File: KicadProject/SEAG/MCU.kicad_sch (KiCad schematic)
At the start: 13 parts, among them J2 Conn_01x06_Pin, SW1 SW_SPDT, U1 STM32F722RCTx, Y1 Crystal_GND24

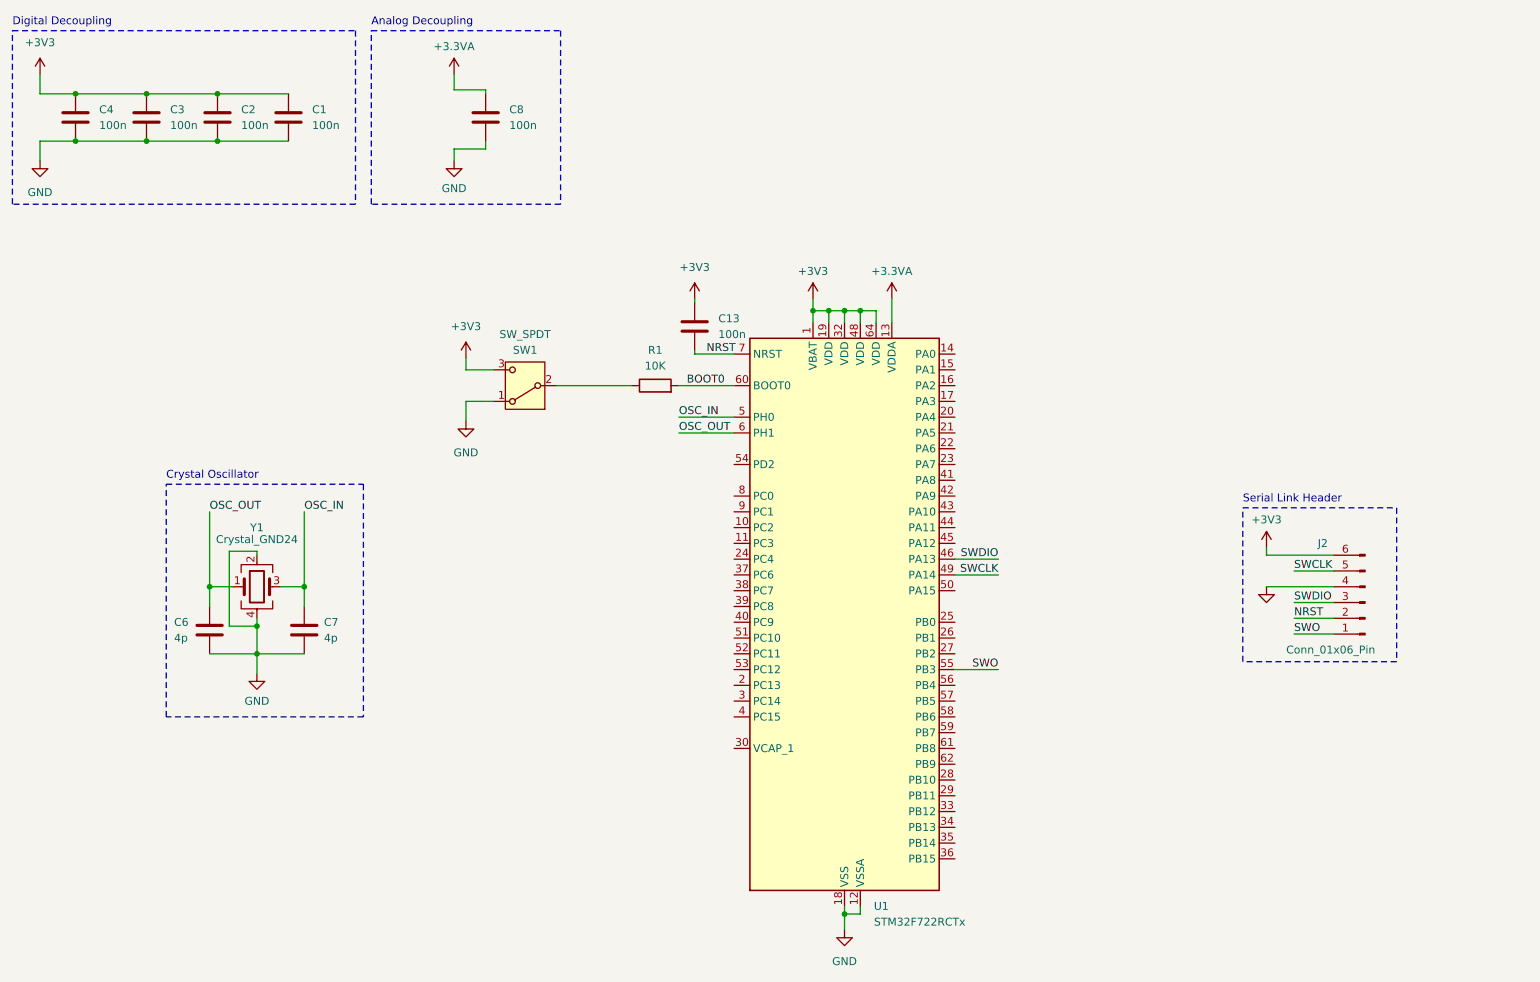
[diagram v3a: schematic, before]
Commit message: Finished PCB, stil uncertain about couple things
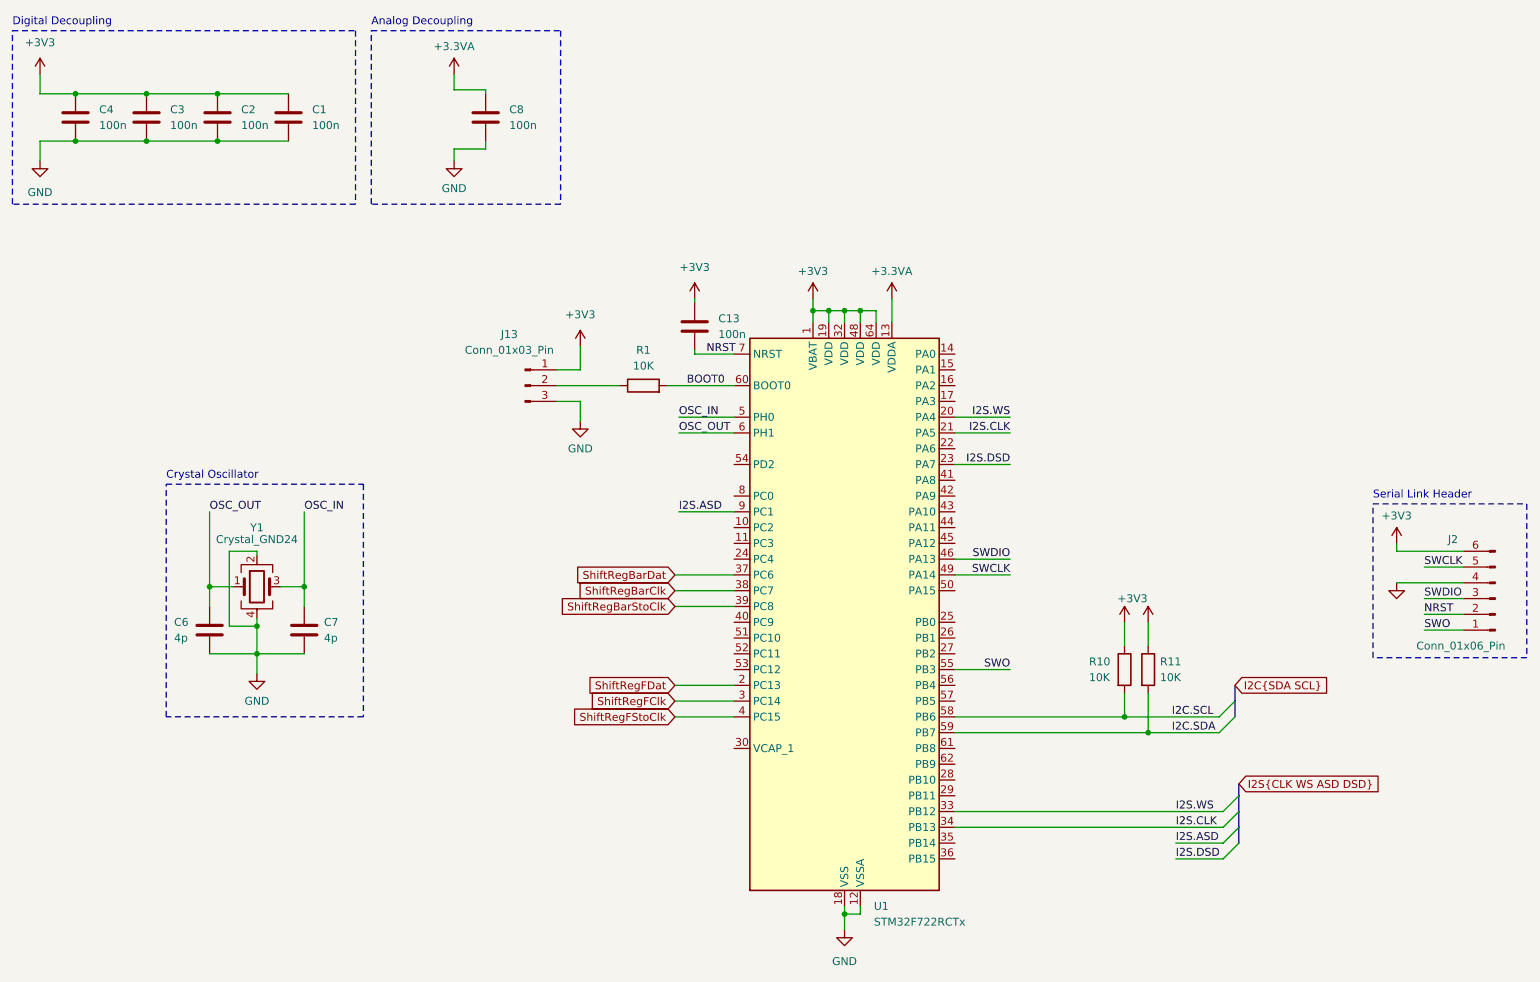
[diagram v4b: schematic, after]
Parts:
- removed SW1: SW_SPDT, symbol Switch:SW_SPDT
- added J13: Conn_01x03_Pin, Connector_PinHeader_2.54mm:PinHeader_1x03_P2.54mm_Vertical, symbol Connector:Conn_01x03_Pin
- added R10, R11: 10K, Resistor_SMD:R_0805_2012Metric, symbol Device:R
- Y1: footprint (none) -> SamacSys_Parts:FW2500025Z
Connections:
- net +3V3: now also J13.1 (Pin_1), R10.1, R11.1
- net GND: now also J13.3 (Pin_3)
- net at R1.1: now also J13.2 (Pin_2)
- net ShiftRegFDat: now reaches U1.2 (PC13)
- net I2S.WS: now reaches U1.20 (PA4)
- net I2S.WS: now also U1.33 (PB12)
- net I2S.CLK: now reaches U1.21 (PA5)
- net I2S.CLK: now also U1.34 (PB13)
- net I2S.DSD: now reaches U1.23 (PA7)
- net ShiftRegFClk: now reaches U1.3 (PC14)
- net ShiftRegBarDat: now reaches U1.37 (PC6)
- net ShiftRegBarClk: now reaches U1.38 (PC7)
- net ShiftRegBarStoClk: now reaches U1.39 (PC8)
- net ShiftRegFStoClk: now reaches U1.4 (PC15)
- net I2C.SCL: now reaches U1.58 (PB6)
- net I2C.SCL: now also R10.2
- net I2C.SDA: now reaches U1.59 (PB7)
- net I2C.SDA: now also R11.2
- net I2S.ASD: now reaches U1.9 (PC1)
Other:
- moved on the sheet: J2, R1

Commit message: PCB rev 2
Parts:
- removed J13: Conn_01x03_Pin, Connector_PinHeader_2.54mm:PinHeader_1x03_P2.54mm_Vertical, symbol Connector:Conn_01x03_Pin
- added C305: 100n, Capacitor_SMD:C_0805_2012Metric, symbol Device:C
- added C309: 4.7u, Capacitor_SMD:C_0805_2012Metric, symbol Device:C
- added H1, H2, H3, H4: MountingHole, MountingHole:MountingHole_3mm, symbol Mechanical:MountingHole
- renumbered C4 to C301, C3 to C302, C2 to C303, C1 to C304, C8 to C306, C6 to C307, C7 to C308, R1 to R301, R10 to R302, R11 to R303
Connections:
- net +3V3: now also C305.1
- net GND: now also R301.1, C305.2, C309.2
- net ShiftRegBarClk: now also U1.10 (PC2); no longer U1.38 (PC7)
- net ShiftRegBarDat: now also U1.8 (PC0); no longer U1.37 (PC6)
- net ShiftRegBarStoClk: now also U1.11 (PC3); no longer U1.39 (PC8)
- net MCLK: now reaches U1.24 (PC4)
- net at U1.30 (VCAP_1): now also C309.1
- net ToggleInput2: now reaches U1.42 (PA9)
- net ToggleInput1: now reaches U1.43 (PA10)
- net ToggleInput4: now reaches U1.44 (PA11)
- net ToggleInput3: now reaches U1.45 (PA12)
- net ToggleInput8: now reaches U1.50 (PA15)
- net ToggleInput7: now reaches U1.51 (PC10)
- net ToggleInput6: now reaches U1.52 (PC11)
- net ToggleInput5: now reaches U1.53 (PC12)
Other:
- moved on the sheet: C306, J2

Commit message: Slight PCB changes
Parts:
- removed H1, H2, H3, H4: MountingHole, MountingHole:MountingHole_3mm, symbol Mechanical:MountingHole
- added C311: 1u, Capacitor_SMD:C_0805_2012Metric, symbol Device:C
- renumbered C13 to C310
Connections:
- net +3V3: now also C311.1
- net GND: now also C311.2
- net RotEncoderIn1: now reaches U1.37 (PC6)
- net RotEncoderIn2: now reaches U1.38 (PC7)
- net RotEncoderButton: now reaches U1.39 (PC8)
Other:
- moved on the sheet: C306

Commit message: Added header
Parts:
- added J9: Conn_01x06_Pin, Connector_PinHeader_2.54mm:PinHeader_1x06_P2.54mm_Vertical, symbol Connector:Conn_01x06_Pin
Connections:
- net I2C.SCL: now also J9.1 (Pin_1)
- net I2C.SDA: now also J9.2 (Pin_2)
- net I2S.ASD: now also J9.4 (Pin_4)
- net I2S.CLK: now also J9.6 (Pin_6)
- net I2S.DSD: now also J9.3 (Pin_3)
- net I2S.WS: now also J9.5 (Pin_5)
- no-connect marks 0 -> 19
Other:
- note added: "Bus Debug"
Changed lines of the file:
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@@
   (junction (at 42.545 30.48) (diameter 0) (color 0 0 0 0)
   )
+  (no_connect (at 172.72 140.97))
+  (no_connect (at 172.72 125.73))
+  (no_connect (at 172.72 87.63))
+  (no_connect (at 172.72 138.43))
+  (no_connect (at 172.72 135.89))
+  (no_connect (at 172.72 77.47))
+  (no_connect (at 172.72 115.57))
+  (no_connect (at 172.72 118.11))
+  (no_connect (at 137.16 90.17))
+  (no_connect (at 172.72 92.71))
+  (no_connect (at 137.16 115.57))
+  (no_connect (at 172.72 72.39))
+  (no_connect (at 172.72 80.01))
+  (no_connect (at 172.72 120.65))
+  (no_connect (at 172.72 153.67))
+  (no_connect (at 172.72 143.51))
+  (no_connect (at 172.72 151.13))
+  (no_connect (at 172.72 128.27))
+  (no_connect (at 172.72 74.93))
   (bus_entry (at 218.44 146.05) (size -2.54 2.54)
     (stroke (width 0) (type default))
   )
+  (bus_entry (at 243.84 61.595) (size 2.54 2.54)
+    (stroke (width 0) (type default))
+  )
+  (bus_entry (at 243.84 64.135) (size 2.54 2.54)
+    (stroke (width 0) (type default))
+  )
   (bus_entry (at 218.44 148.59) (size -2.54 2.54)
     (stroke (width 0) (type default))
@@
     (stroke (width 0) (type default))
   )
+  (bus_entry (at 243.84 59.055) (size 2.54 2.54)
+    (stroke (width 0) (type default))
+  )
+  (bus_entry (at 243.84 56.515) (size 2.54 2.54)
+    (stroke (width 0) (type default))
+  )
+  (bus_entry (at 243.84 51.435) (size 2.54 2.54)
+    (stroke (width 0) (type default))
+  )
+  (bus_entry (at 243.84 53.975) (size 2.54 2.54)
+    (stroke (width 0) (type default))
+  )
   (wire (pts (xy 127.635 107.95) (xy 137.16 107.95))
     (stroke (width 0) (type default))
   )
+  (wire (pts (xy 246.38 61.595) (xy 254.635 61.595))
+    (stroke (width 0) (type default))
+  )
   (wire (pts (xy 208.28 153.67) (xy 215.9 153.67))
     (stroke (width 0) (type default))
@@
     (stroke (width 0) (type default))
   )
+  (wire (pts (xy 246.38 66.675) (xy 254.635 66.675))
+    (stroke (width 0) (type default))
+  )
   (wire (pts (xy 203.835 127) (xy 203.835 133.35))
     (stroke (width 0) (type default))
@@
     (stroke (width 0) (type default))
   )
+  (wire (pts (xy 246.38 53.975) (xy 254.635 53.975))
+    (stroke (width 0) (type default))
+  )
   (wire (pts (xy 243.84 97.155) (xy 254.635 97.155))
     (stroke (width 0) (type default))
@@
     (stroke (width 0) (type default))
   )
+  (bus (pts (xy 243.84 53.975) (xy 243.84 56.515))
+    (stroke (width 0) (type default))
+  )
   (wire (pts (xy 25.4 27.305) (xy 25.4 30.48))
     (stroke (width 0) (type default))
@@
     (stroke (width 0) (type default))
   )
+  (bus (pts (xy 243.84 48.895) (xy 243.84 51.435))
+    (stroke (width 0) (type default))
+  )
   (wire (pts (xy 126.365 38.1) (xy 126.365 39.37))
     (stroke (width 0) (type default))
@@
     (stroke (width 0) (type default))
   )
+  (bus (pts (xy 243.84 56.515) (xy 243.84 59.055))
+    (stroke (width 0) (type default))
+  )
   (wire (pts (xy 160.02 65.405) (xy 160.02 67.31))
     (stroke (width 0) (type default))
@@
     (stroke (width 0) (type default))
   )
+  (wire (pts (xy 246.38 64.135) (xy 254.635 64.135))
+    (stroke (width 0) (type default))
+  )
   (wire (pts (xy 200.025 117.475) (xy 200.025 119.38))
     (stroke (width 0) (type default))
@@
     (stroke (width 0) (type default))
   )
+  (bus (pts (xy 243.84 61.595) (xy 243.84 64.135))
+    (stroke (width 0) (type default))
+  )
   (wire (pts (xy 31.115 30.48) (xy 42.545 30.48))
     (stroke (width 0) (type default))
@@
     (stroke (width 0) (type default))
   )
+  (bus (pts (xy 243.84 51.435) (xy 243.84 53.975))
+    (stroke (width 0) (type default))
+  )
   (wire (pts (xy 157.48 162.56) (xy 157.48 161.29))
     (stroke (width 0) (type default))
@@
     (stroke (width 0) (type default))
   )
+  (wire (pts (xy 246.38 56.515) (xy 254.635 56.515))
+    (stroke (width 0) (type default))
+  )
   (wire (pts (xy 172.72 146.05) (xy 215.9 146.05))
     (stroke (width 0) (type default))
   )
   (wire (pts (xy 60.325 114.935) (xy 60.325 116.205))
+    (stroke (width 0) (type default))
+  )
+  (wire (pts (xy 246.38 59.055) (xy 254.635 59.055))
+    (stroke (width 0) (type default))
+  )
+  (bus (pts (xy 243.84 60.96) (xy 243.84 61.595))
     (stroke (width 0) (type default))
   )
@@
     (fill (type none))
   )
+  (rectangle (start 218.44 46.355) (end 262.89 71.12)
+    (stroke (width 0) (type dash))
+    (fill (type none))
+  )
   (rectangle (start 240.03 89.535) (end 264.795 114.3)
     (stroke (width 0) (type dash))
@@
     (effects (font (size 1.27 1.27)) (justify left bottom))
   )
+  (text "Bus Debug" (at 218.44 45.72 0)
+    (effects (font (size 1.27 1.27)) (justify left bottom))
+  )
   (label "OSC_IN" (at 67.945 97.79 0) (fields_autoplaced)
     (effects (font (size 1.27 1.27)) (justify left bottom))
@@
     (effects (font (size 1.27 1.27)) (justify right bottom))
   )
+  (label "I2S.CLK" (at 246.38 53.975 0)
+    (effects (font (size 1.27 1.27)) (justify left bottom))
+  )
   (label "I2S.DSD" (at 181.61 90.17 180) (fields_autoplaced)
     (effects (font (size 1.27 1.27)) (justify right bottom))
@@
     (effects (font (size 1.27 1.27)) (justify right bottom))
   )
+  (label "I2S.DSD" (at 246.38 61.595 0)
+    (effects (font (size 1.27 1.27)) (justify left bottom))
+  )
   (label "SWCLK" (at 248.285 99.695 0) (fields_autoplaced)
     (effects (font (size 1.27 1.27)) (justify left bottom))
@@
   )
   (label "BOOT0" (at 129.54 77.47 0) (fields_autoplaced)
+    (effects (font (size 1.27 1.27)) (justify left bottom))
+  )
+  (label "I2C.SDA" (at 246.38 64.135 0)
     (effects (font (size 1.27 1.27)) (justify left bottom))
   )
@@
     (effects (font (size 1.27 1.27)) (justify left bottom))
   )
+  (label "I2S.ASD" (at 246.38 59.055 0)
+    (effects (font (size 1.27 1.27)) (justify left bottom))
+  )
   (label "NRST" (at 248.285 107.315 0) (fields_autoplaced)
     (effects (font (size 1.27 1.27)) (justify left bottom))
@@
     (effects (font (size 1.27 1.27)) (justify left bottom))
   )
+  (label "I2C.SCL" (at 246.38 66.675 0)
+    (effects (font (size 1.27 1.27)) (justify left bottom))
+  )
   (label "OSC_OUT" (at 128.27 85.09 0) (fields_autoplaced)
+    (effects (font (size 1.27 1.27)) (justify left bottom))
+  )
+  (label "I2S.WS" (at 246.38 56.515 0)
     (effects (font (size 1.27 1.27)) (justify left bottom))
   )
@@
     )
   )
+  (global_label "I2S{CLK WS ASD DSD}" (shape input) (at 243.84 48.895 180) (fields_autoplaced)
+    (effects (font (size 1.27 1.27)) (justify right))
+    (property "Intersheetrefs" "${INTERSHEET_REFS}" (at 219.6882 48.895 0)
+      (effects (font (size 1.27 1.27)) (justify right) hide)
+    )
+  )
   (global_label "MCLK" (shape input) (at 127.635 105.41 180) (fields_autoplaced)
     (effects (font (size 1.27 1.27)) (justify right))
@@
     )
   )
+  (global_label "I2C{SDA SCL}" (shape input) (at 243.84 60.96 180) (fields_autoplaced)
+    (effects (font (size 1.27 1.27)) (justify right))
+    (property "Intersheetrefs" "${INTERSHEET_REFS}" (at 228.0338 60.96 0)
+      (effects (font (size 1.27 1.27)) (justify right) hide)
+    )
+  )
   (global_label "RotEncoderButton" (shape input) (at 127.635 113.03 180) (fields_autoplaced)
     (effects (font (size 1.27 1.27)) (justify right))
@@
       (effects (font (size 1.27 1.27)) (justify right))
     )
-    (property "Value" "Conn_01x06_Pin" (at 247.015 112.395 0)
+    (property "Value" "Conn_01x06_Pin" (at 245.745 112.395 0)
       (effects (font (size 1.27 1.27)) (justify right))
     )
@@
         )
       )
+    )
+  )
+  (symbol (lib_id "Connector:Conn_01x06_Pin") (at 259.715 61.595 180) (unit 1)
+    (in_bom yes) (on_board yes) (dnp no)
+    (property "Reference" "J9" (at 255.27 50.8 0)
+      (effects (font (size 1.27 1.27)) (justify right))
+    )
+    (property "Value" "Conn_01x06_Pin" (at 245.745 69.215 0)
+      (effects (font (size 1.27 1.27)) (justify right))
+    )
+    (property "Footprint" "Connector_PinHeader_2.54mm:PinHeader_1x06_P2.54mm_Vertical" (at 259.715 61.595 0)
+      (effects (font (size 1.27 1.27)) hide)
+    )
+    (property "Datasheet" "~" (at 259.715 61.595 0)
+      (effects (font (size 1.27 1.27)) hide)
+    )
+    (pin "3")
+    (pin "4")
+    (pin "6")
+    (pin "2")
+    (pin "5")
+    (pin "1")
+    (instances
+      (project "SEAG"
+        (path "/37e7da6e-dab5-4e62-b28a-754ec4806405/73c774ae-3af2-431c-8167-2f494c9438a8"
+          (reference "J9") (unit 1)
+        )
+      )
